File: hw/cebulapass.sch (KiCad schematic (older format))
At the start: 2 parts, among them U1 NRF24L01_Breakout, U2 STM32F070CBTx

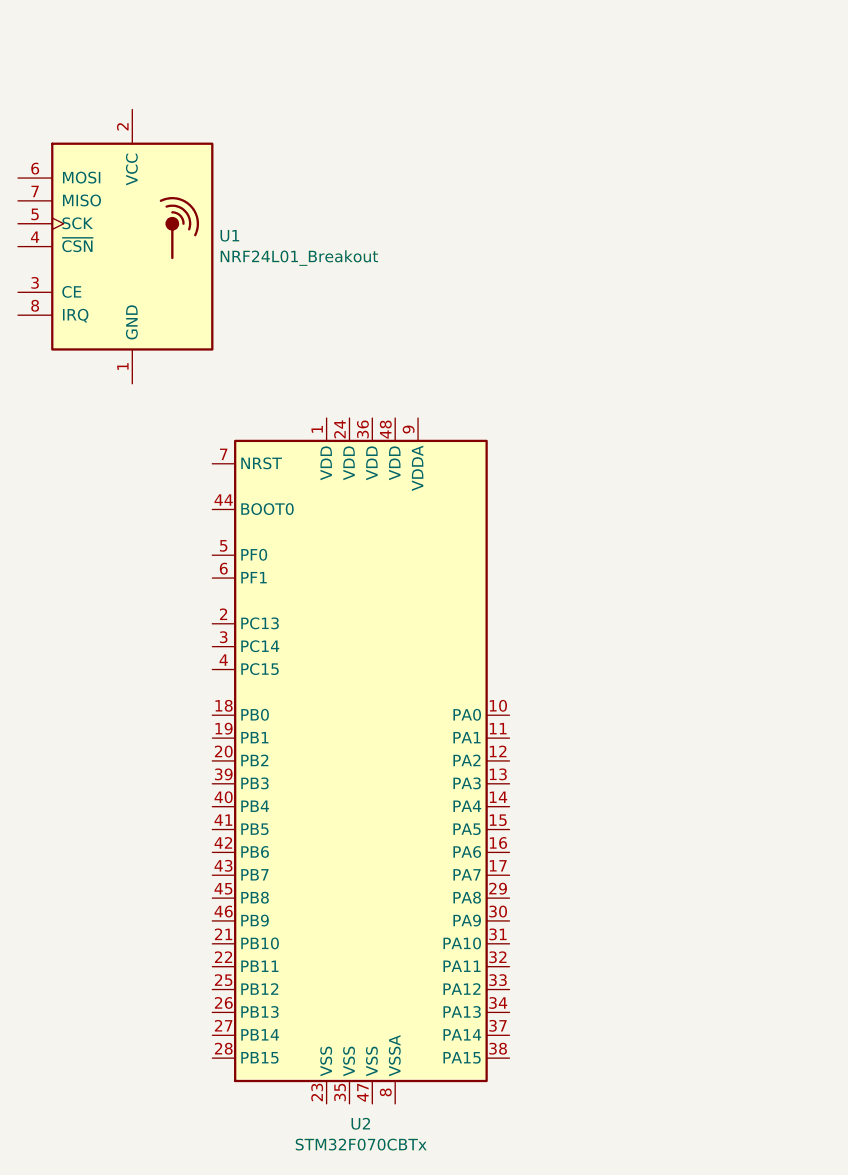
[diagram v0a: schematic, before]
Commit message: Adding nRF24 and USB-on-PCB
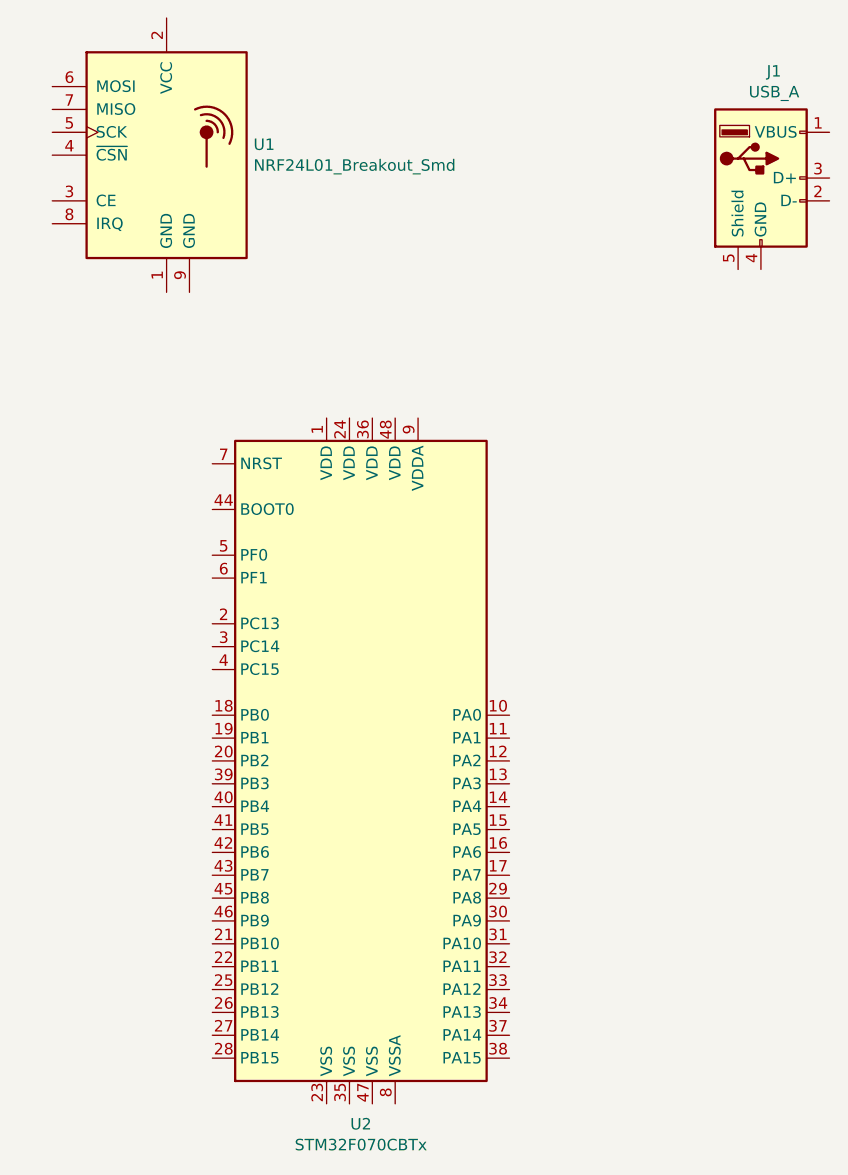
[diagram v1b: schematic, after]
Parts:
- removed U1: NRF24L01_Breakout, RF_Module:nRF24L01_Breakout, symbol RF:NRF24L01_Breakout
- added J1: USB_A, Connector_USB:USB_A_Pads_On_PCB, symbol Connector:USB_A
- added U1: NRF24L01_Breakout_Smd, RF_Module:nRF24L01_Breakout_Smd, symbol RF:NRF24L01_Breakout_Smd
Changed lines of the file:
@@
 EESchema Schematic File Version 4
+LIBS:cebulapass-cache
 EELAYER 30 0
 EELAYER END
@@
 $EndDescr
 $Comp
-L RF:NRF24L01_Breakout U1
-U 1 1 5D9A23EC
-P 3050 2150
-F 0 "U1" H 3430 2196 50  0000 L CNN
-F 1 "NRF24L01_Breakout" H 3430 2105 50  0000 L CNN
-F 2 "RF_Module:nRF24L01_Breakout" H 3200 2750 50  0001 L CIN
-F 3 "http://www.nordicsemi.com/eng/content/download/2730/34105/file/nRF24L01_Product_Specification_v2_0.pdf" H 3050 2050 50  0001 C CNN
-	1    3050 2150
-	1    0    0    -1
-$EndComp
-$Comp
 L MCU_ST_STM32F0:STM32F070CBTx U2
 U 1 1 5D9B1A7A
@@
 	1    0    0    -1
 $EndComp
+$Comp
+L RF:NRF24L01_Breakout_Smd U1
+U 1 1 5DAD72F4
+P 3200 1750
+F 0 "U1" H 3580 1796 50  0000 L CNN
+F 1 "NRF24L01_Breakout_Smd" H 3580 1705 50  0000 L CNN
+F 2 "RF_Module:nRF24L01_Breakout_Smd" H 3350 2350 50  0001 L CIN
+F 3 "http://www.nordicsemi.com/eng/content/download/2730/34105/file/nRF24L01_Product_Specification_v2_0.pdf" H 3200 1650 50  0001 C CNN
+	1    3200 1750
+	1    0    0    -1
+$EndComp
+$Comp
+L Connector:USB_A J1
+U 1 1 5DAC935D
+P 5800 1850
+F 0 "J1" H 5857 2317 50  0000 C CNN
+F 1 "USB_A" H 5857 2226 50  0000 C CNN
+F 2 "Connector_USB:USB_A_Pads_On_PCB" H 5950 1800 50  0001 C CNN
+F 3 " ~" H 5950 1800 50  0001 C CNN
+	1    5800 1850
+	1    0    0    -1
+$EndComp
